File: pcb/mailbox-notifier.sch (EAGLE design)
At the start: 24 parts, among them Q1 AO3401, U1 MIC23155, U2 LTC2943-X, U3 FS312F-G, U4 FS8205, U5 MCP73832, U6 EFM32PG1B200_Q32, U7 RFM69HW

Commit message: PCB Work
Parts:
- removed U4: FS8205, Fortune:FS8205
- added C4: 100uF, Capacitor:CAPACITOR-1206
- added C49: 100nF, Capacitor:CAPACITOR-0603
- added CON1: 3P-SH-SIDE, JST:3P-SH-SIDE
- added D2: SMAJ5.0A, TVS:SMAJ5.0A
- added F1: 1A Hold, PTC Fuses:PTC1206
- added R1, R2: 5.1K Ohms, Resistor:RESISTOR-0603
- added R58: 1K Ohms, Resistor:RESISTOR-0603
- added R59: 100 Ohms, Resistor:RESISTOR-0603
- added R63: 10M Ohm, Resistor:RESISTOR-0603
- added U14: FS312F-G, Fortune:FS312F-G
- added U16: FS8205, Fortune:FS8205
- added U8: SI7021, Silicon Labs:SI7021
- U3: value FS312F-G -> 74LVC1G17; device Fortune:FS312F-G -> Logic:74LVC1G17
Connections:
- new net 5V0: C4.C1, D1.A, D2.C, F1.1, Q1.G
- new net EXT_TRIG: U3.1.Y
- new net GBAT: BAT1.-, C49.C2, R63.2, U14.GND, U16.S2
- new net N$2: BAT1.+, U2.VBAT/SENSE-
- new net N$3: R1.2, USB1.CC2
- new net N$4: F1.2, USB1.VBUS
- new net N$47: U14.OC, U16.G1
- new net N$48: U14.OD, U16.G2
- new net N$49: R59.1, U14.VCC
- new net N$5: R2.2, USB1.CC1
- new net N$50: R58.1, U14.CS
- new net N$6: CON1-2.S, U3.1.A
- new net VBAT: C49.C1, Q1.D, R59.2, U2.VDD/SENSE+
- new net VIN: D1.C, Q1.S
- net 2V8: now also CON1-1.S, U3.PWR.VCC
- net GND: now also C4.C2, CON1-3.S, D2.A, R1.1, R2.1, R58.2, R63.1, U16.S1, U3.PWR.GND, USB1.GND, USB1.SHIELD@0, USB1.SHIELD@1, USB1.SHIELD@2, USB1.SHIELD@3
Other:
- note added: "Decouple"

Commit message: PCB work
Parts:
- removed C49: 100nF, Capacitor:CAPACITOR-0603
- removed R58: 1K Ohms, Resistor:RESISTOR-0603
- removed R59: 100 Ohms, Resistor:RESISTOR-0603
- removed R63: 10M Ohm, Resistor:RESISTOR-0603
- removed U14: FS312F-G, Fortune:FS312F-G
- removed U16: FS8205, Fortune:FS8205
- removed U2: LTC2943-X, Analog Devices:LTC2943-X
- added C10: 2.2uF, Capacitor:CAPACITOR-0603
- added C11: 100uF, Capacitor:CAPACITOR-1206
- added C12, C14, C15, C20, C21, C23, C7: 100nF, Capacitor:CAPACITOR-0603
- added C17, C24: 1uF, Capacitor:CAPACITOR-0603
- added C22, C9: 470pF, Capacitor:CAPACITOR-0603
- added C5, C6: 10uF, Capacitor:CAPACITOR-0603
- added C8: 4.7uF, Capacitor:CAPACITOR-0603
- added D3: SK9822, LED:SK9822
- added L2: 4.7uH, Inductor:INDUCTOR-0603
- added R10: 324K Ohms, Resistor:RESISTOR-0603
- added R11: 91K Ohms, Resistor:RESISTOR-0603
- added R12: 10M Ohm, Resistor:RESISTOR-0603
- added R15: 10K Ohms, Resistor:RESISTOR-0603
- added R16, R17, R18, R19, R20, R9: 100K Ohms, Resistor:RESISTOR-0603
- added R21: 2K Ohms, Resistor:RESISTOR-0603
- added R3: 5.1K Ohms, Resistor:RESISTOR-0603
- added R7: 1K Ohms, Resistor:RESISTOR-0603
- added R8: 100 Ohms, Resistor:RESISTOR-0603
- added U10: SI7021, Silicon Labs:SI7021
- added U12: MIC2019, Microchip:MIC2019
- added U4: MIC23155, Microchip:MIC23155
- added U9: RFM69HW, HopeRF:RFM69HW
- added X1: 40MHz, Crystal:CRYSTAL_4P
- C16: value 100nF -> 4.7uF
- C18: value 1uF -> 100nF
- C19: value 4.7uF -> 100nF
- C2: value 100nF -> 100uF; device Capacitor:CAPACITOR-0603 -> Capacitor:CAPACITOR-1206
- D1: value B0530W -> SMAJ5.0A; device Generic Diode:B0530W -> TVS:SMAJ5.0A
- D2: value SMAJ5.0A -> B0530W; device TVS:SMAJ5.0A -> Generic Diode:B0530W
- L1: value 4.7uH -> 2.2uH; device Inductor:INDUCTOR-0603 -> Inductor:INDUCTOR-0805; OCLCSC C281111 -> C139241
- R13, R4: value 10K Ohms -> 100K Ohms
- R2: value 5.1K Ohms -> 2.2K Ohms
- U1: value MIC23155 -> MCP73832; device Microchip:MIC23155 -> Microchip:MCP73832
- U5: value MCP73832 -> FS312F-G; device Microchip:MCP73832 -> Fortune:FS312F-G
- U6: value EFM32PG1B200_Q32 -> FS8205; device EFM32:EFM32PG1B200_Q32 -> Fortune:FS8205
- U7: value RFM69HW -> EFM32PG1B200_Q32; device HopeRF:RFM69HW -> EFM32:EFM32PG1B200_Q32
- U8: value SI7021 -> SST26VF016B; device Silicon Labs:SI7021 -> Microchip:SST26VF016B
- renumbered C1 to C13, U3 to U11
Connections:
- removed net N$2: BAT1.+, U2.VBAT/SENSE-
- new net !FLASH_CS: R16.1, U8.!CS!
- new net 2V8_PGOOD: R9.1, U4.PG
- new net BAT_STAT: R4.1, U1.STAT
- new net I2C0_SCL: R15.1, U10.SCL
- new net I2C0_SDA: R14.1, U10.SDA
- new net LED_EN: U12.EN
- new net N$10: R2.2, U1.PROG
- new net N$11: R21.2, U12.ILIMIT
- new net N$12: L1.1, U4.SW
- new net N$13: R10.1, R11.2, U4.FB
- new net N$14: C9.C1, U4.SS
- new net N$15: C24.C1, D3.VDD@5, U12.VOUT
- new net N$16: U7.HFXTAL_N, X1.1
- new net N$17: U7.HFXTAL_P, X1.2
- new net US1_CLK: D3.CLKI@4
- new net US1_MOSI: D3.SDI@3
- new net VBAT_SENSE: C22.C1, R19.1, R20.2
- new net VIN1: C3.C1
- net !RFM_CS: now also R18.1, U7.PD12, U9.!CS; no longer R14.1, U6.PD12, U7.!CS
- net !RST: now also R13.1, U7.!RESET; no longer R4.1, U6.!RESET
- net 1V8: now also C16.C1, L2.1, U7.DVDD; no longer C19.C1, L1.1, U6.DVDD
- net 2V8: now also C10.C1, C11.C1, C14.C1, C15.C1, C18.C1, C19.C2, C20.C1, C21.C1, C23.C1, L1.2, R10.2, R13.2, R15.2, R16.2, R18.2, R9.2, U10.VDD, U12.VIN, U4.SNS, U7.AVDD@0, U7.AVDD@1, U7.IOVDD0@0, U7.VREGVDD, U8.!HOLD!/IO3, U8.!WP!/IO2, U8.VCC, U9.VCC; no longer C16.C2, C2.C1, C3.C1, U6.AVDD@0, U6.AVDD@1, U6.IOVDD0@0, U6.VREGVDD, U7.VCC
- net 5V0: now also C2.C1, D1.C, D2.A, U1.VDD; no longer C4.C1, D1.A, D2.C
- net GBAT: now also C12.C2, R12.2, U5.GND, U6.S2; no longer C49.C2, R63.2, U14.GND, U16.S2
- net GND: now also C10.C2, C11.C2, C14.C2, C15.C2, C16.C2, C17.C1, C18.C2, C19.C1, C20.C2, C21.C2, C22.C2, C23.C2, C24.C2, C5.C2, C6.C2, C7.C2, C8.C2, C9.C2, D1.A, D3.GND@2, R11.1, R12.1, R17.1, R20.1, R21.1, R3.1, R7.1, U1.VSS, U10.GND, U12.GND, U4.AGND, U4.PGND@0, U4.PGND@1, U6.S1, U7.VREGVSS, U7.VSS@0, U8.GND, U9.GND, X1.GND@0, X1.GND@1; no longer C16.C1, C18.C1, C19.C2, D2.A, R13.1, R58.2, R63.1, U16.S1, U6.VREGVSS, U6.VSS@0, U7.GND
- net N$1: now also U9.ANT; no longer U7.ANT
- net N$19: now also L2.2, U7.VREGSW; no longer L1.2, U6.VREGSW
- net N$20: now also C17.C2, U7.DECOUPLE; no longer C18.C2, U6.DECOUPLE
- net N$47: now also U5.OC, U6.G1; no longer U14.OC, U16.G1
- net N$48: now also U5.OD, U6.G2; no longer U14.OD, U16.G2
- net N$49: now also R8.1, U5.VCC; no longer R59.1, U14.VCC
- net N$5: now also R3.2; no longer R2.2
- net N$50: now also R7.2, U5.CS; no longer R58.1, U14.CS
- net RFM_IRQ: now also U7.PC10, U9.IO0; no longer U6.PC10, U7.IO0
- net RFM_RST: now also R17.2, U7.PD11, U9.RST; no longer R13.2, U6.PD11, U7.RST
- net SWCLK: now also U7.PF0; no longer U6.PF0
- net SWDIO: now also U7.PF1; no longer U6.PF1
- net SWO: now also U7.PF2; no longer U6.PF2
- net US0_CLK: now also U7.PD13, U8.SCK, U9.SCK; no longer U6.PD13, U7.SCK
- net US0_MISO: now also U7.PD15, U8.MISO/IO1, U9.MISO; no longer U6.PD15, U7.MISO
- net US0_MOSI: now also U7.PD14, U8.MOSI/IO0, U9.MOSI; no longer U6.PD14, U7.MOSI
- net VBAT: now also BAT1.+, C12.C1, C4.C1, R19.2, R8.2, U1.VBAT; no longer C49.C1, R59.2, U2.VDD/SENSE+
- net VIN: now also C5.C1, C6.C1, C7.C1, C8.C1, D2.C, U4.EN, U4.VIN@0, U4.VIN@1; no longer D1.C

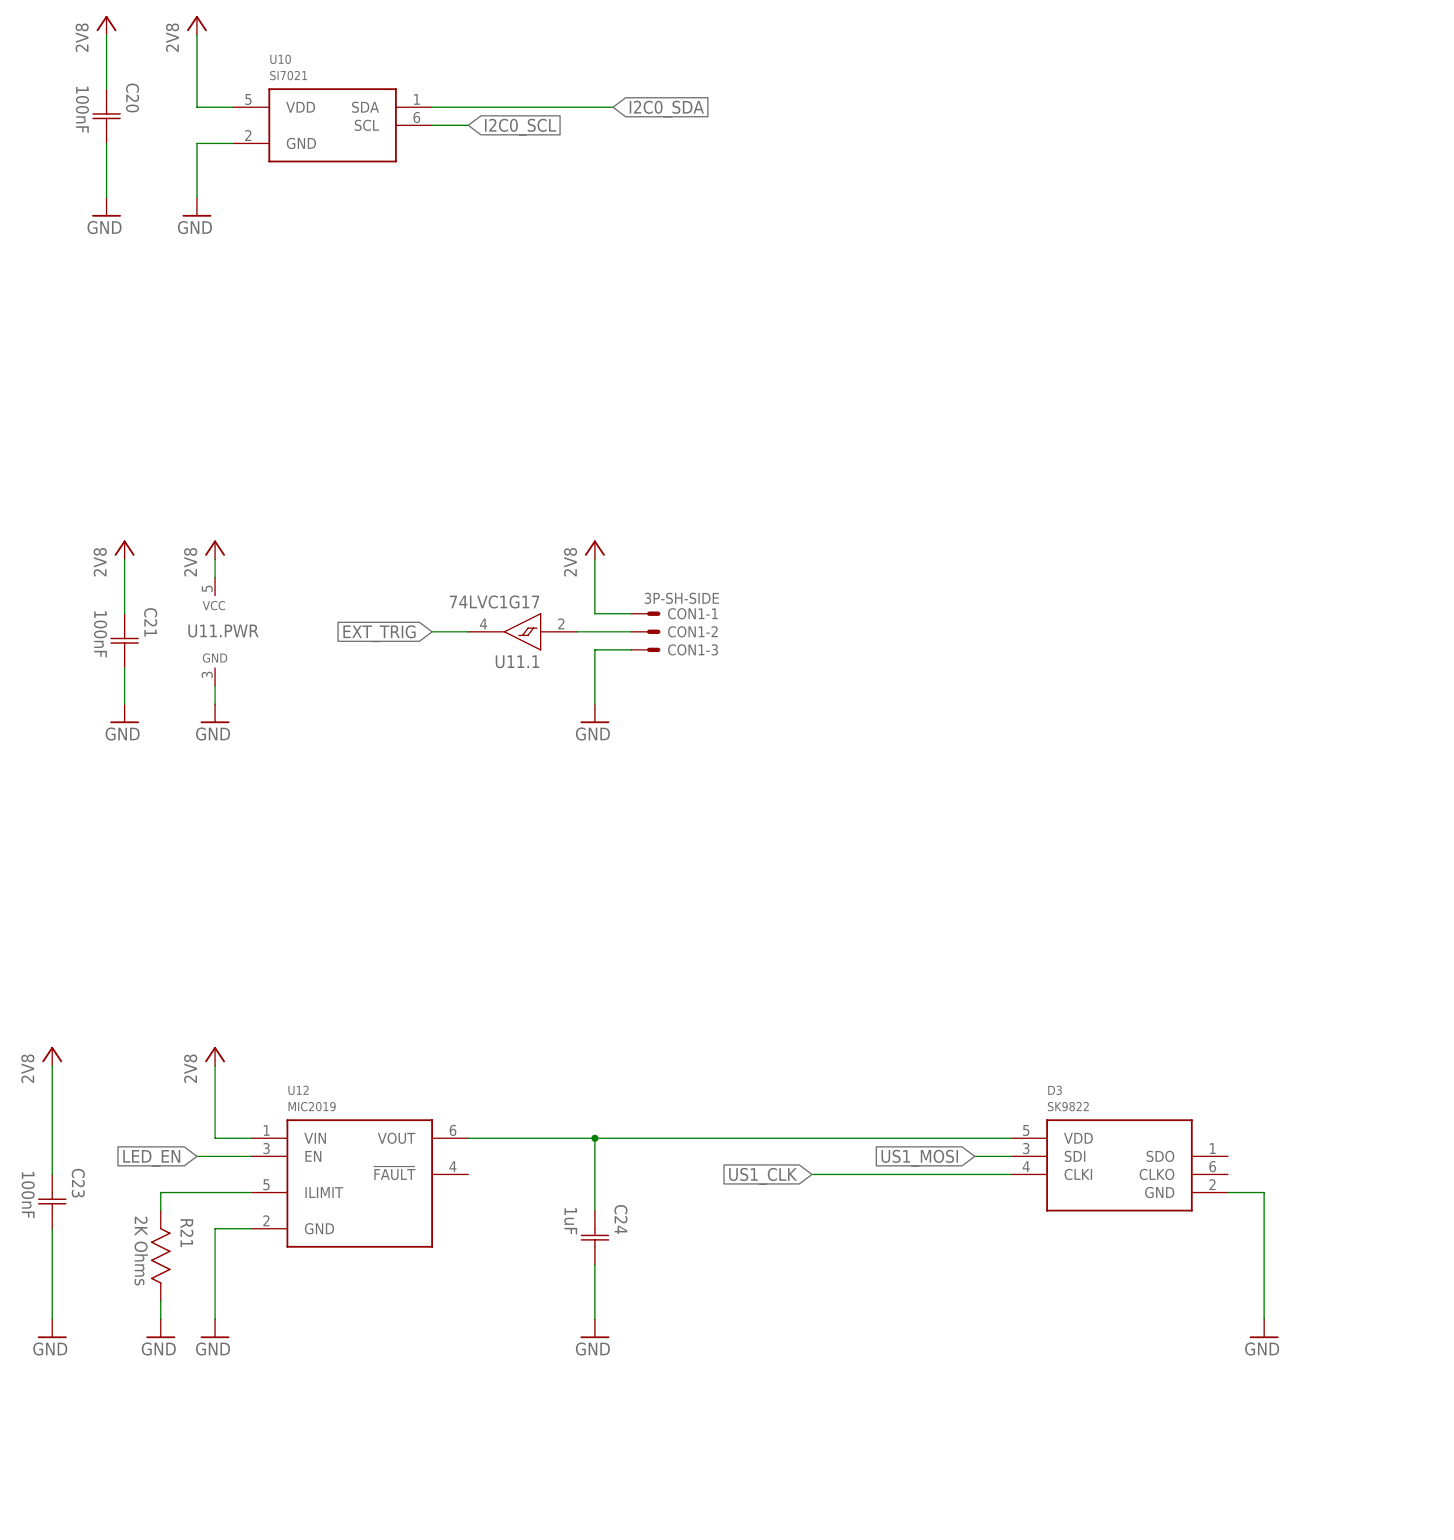
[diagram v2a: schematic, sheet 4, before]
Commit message: Add power switch to external trigger
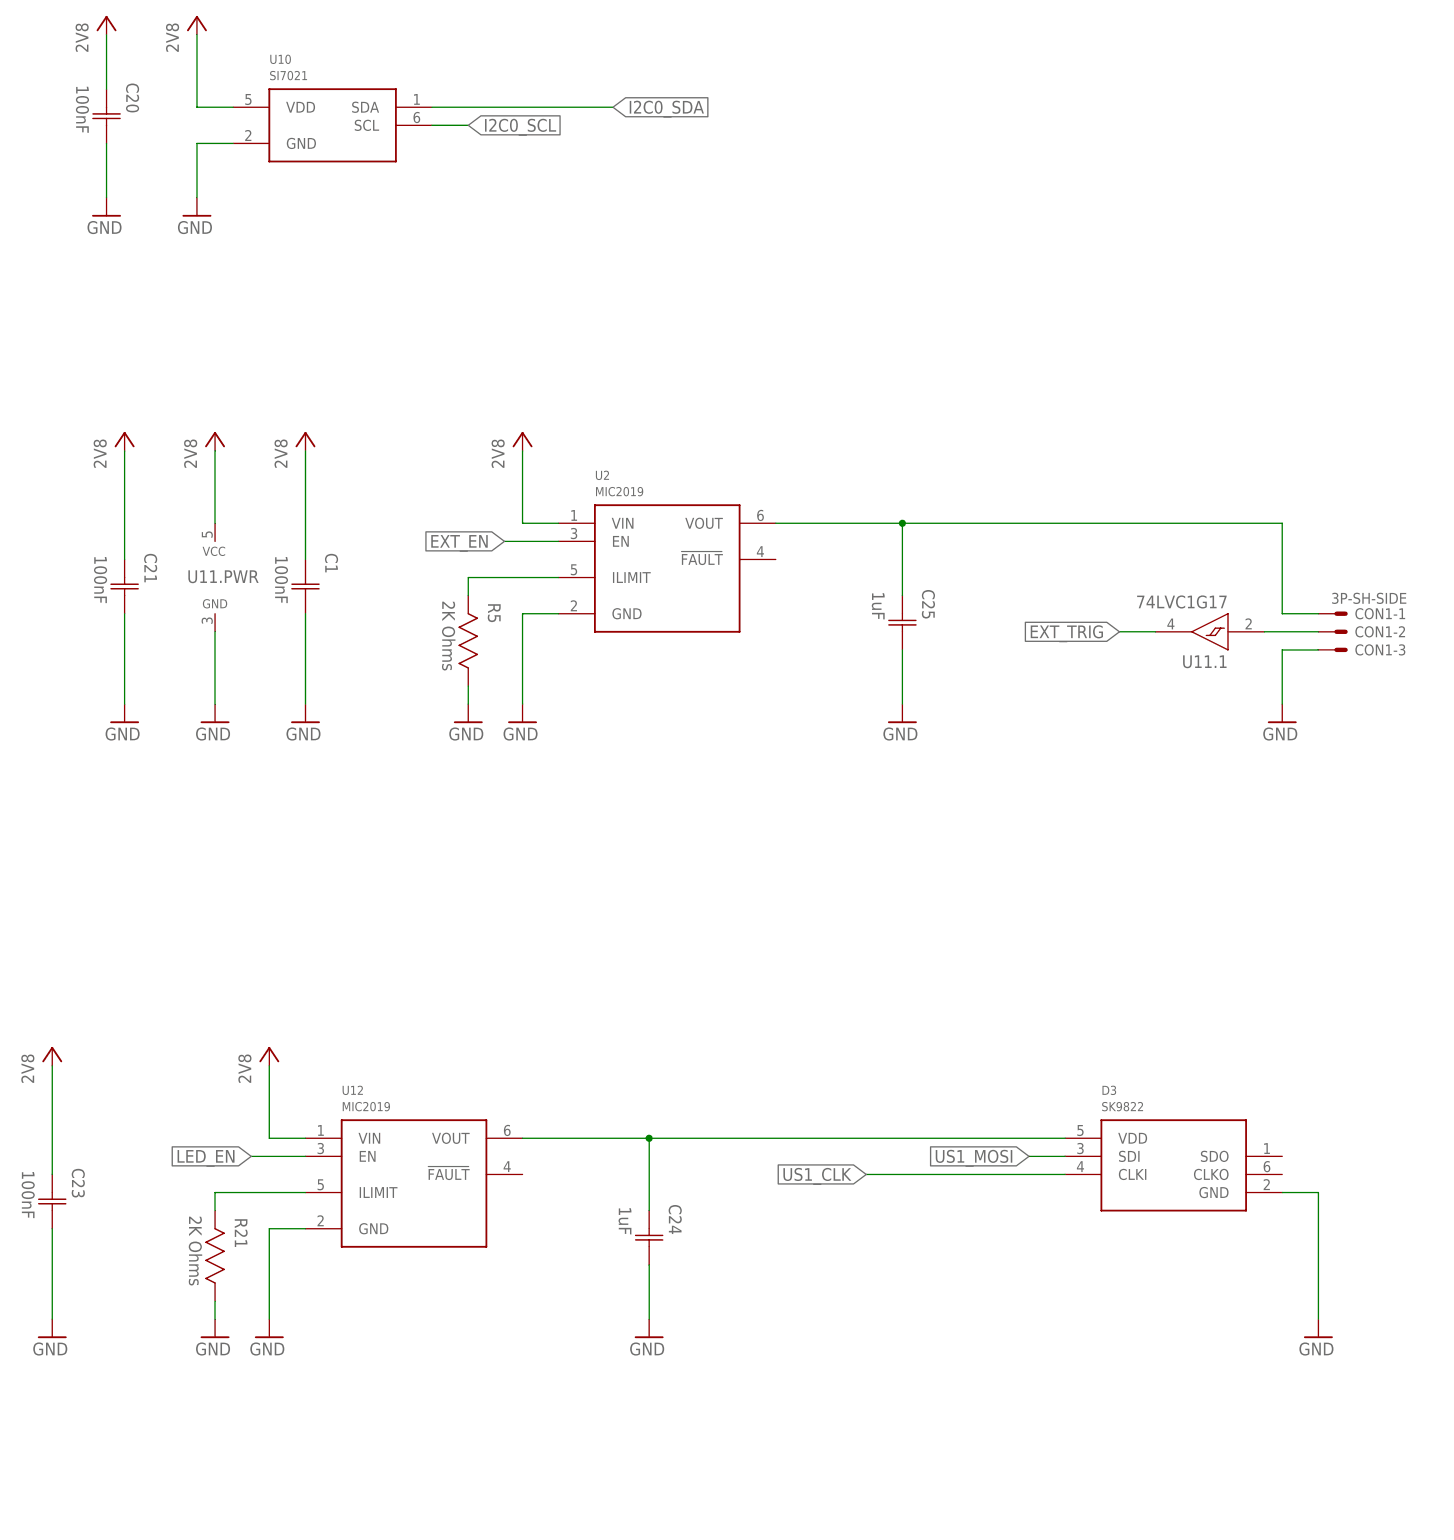
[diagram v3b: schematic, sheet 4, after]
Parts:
- added C1: 100nF, Capacitor:CAPACITOR-0603
- added C25: 1uF, Capacitor:CAPACITOR-0603
- added R5: 2K Ohms, Resistor:RESISTOR-0603
- added U2: MIC2019, Microchip:MIC2019
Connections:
- new net EXT_EN: U2.EN
- new net N$2: R5.2, U2.ILIMIT
- new net N$7: C25.C1, CON1-1.S, U2.VOUT
- net 2V8: now also C1.C1, U2.VIN; no longer CON1-1.S
- net GND: now also C1.C2, C25.C2, R5.1, U2.GND
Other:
- moved on the sheet: C21, C24, CON1-1, CON1-2, CON1-3, D3, R21, U11.1, U11.PWR, U12

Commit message: PCB work
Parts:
- removed C24, C25: 1uF, Capacitor:CAPACITOR-0603
- removed R21: 2K Ohms, Resistor:RESISTOR-0603
- removed U12: MIC2019, Microchip:MIC2019
- added R6: 100K Ohms, Resistor:RESISTOR-0603
- added U3: FS312F-G, Fortune:FS312F-G
- C10: value 2.2uF -> 100uF; device Capacitor:CAPACITOR-0603 -> Capacitor:CAPACITOR-1206
- C11: value 100uF -> 100nF; device Capacitor:CAPACITOR-1206 -> Capacitor:CAPACITOR-0603
- C15: value 100nF -> 4.7uF
- C16: value 4.7uF -> 1uF
- C17: value 1uF -> 100nF
- C22: value 470pF -> 1uF
- C23: value 100nF -> 1uF
- C3: value 100nF -> 100uF; device Capacitor:CAPACITOR-0603 -> Capacitor:CAPACITOR-1206
- C4: value 100uF -> 10uF; device Capacitor:CAPACITOR-1206 -> Capacitor:CAPACITOR-0603
- C6: value 10uF -> 470pF
- C8: value 4.7uF -> 470pF
- C9: value 470pF -> 2.2uF
- R19, R20: value 100K Ohms -> 2K Ohms
- R5: value 2K Ohms -> 100K Ohms
- U10: value SI7021 -> MIC2019; device Silicon Labs:SI7021 -> Microchip:MIC2019
- U2: value MIC2019 -> MIC23155; device Microchip:MIC2019 -> Microchip:MIC23155
- U4: value MIC23155 -> FS8205; device Microchip:MIC23155 -> Fortune:FS8205
- U5: value FS312F-G -> EFM32PG1B200F256GM32; device Fortune:FS312F-G -> EFM32:EFM32PG1B200F256GM32
- U6: value FS8205 -> SST26VF016B; device Fortune:FS8205 -> Microchip:SST26VF016B
- U7: value EFM32PG1B200_Q32 -> RFM69HW; device EFM32:EFM32PG1B200_Q32 -> HopeRF:RFM69HW
- U8: value SST26VF016B -> SI7021; device Microchip:SST26VF016B -> Silicon Labs:SI7021
- U9: value RFM69HW -> MIC2019; device HopeRF:RFM69HW -> Microchip:MIC2019
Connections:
- removed net VIN1: C3.C1
- net !FLASH_CS: now also U5.PD15, U6.!CS!; no longer U8.!CS!
- net !RFM_CS: now also U5.PD13, U7.!CS; no longer U7.PD12, U9.!CS
- net !RST: now also U5.!RESET; no longer U7.!RESET
- net 1V8: now also C15.C1, U5.DVDD; no longer C16.C1, U7.DVDD
- net 2V8: now also C12.C1, C17.C1, C18.C2, C19.C1, C9.C1, U10.VIN, U2.SNS, U5.AVDD@0, U5.AVDD@1, U5.IOVDD0@0, U5.VREGVDD, U6.!HOLD!/IO3, U6.!WP!/IO2, U6.VCC, U7.VCC, U8.VDD, U9.VIN; no longer C1.C1, C11.C1, C15.C1, C18.C1, C19.C2, C23.C1, U10.VDD, U12.VIN, U2.VIN, U4.SNS, U7.AVDD@0, U7.AVDD@1, U7.IOVDD0@0, U7.VREGVDD, U8.!HOLD!/IO3, U8.!WP!/IO2, U8.VCC, U9.VCC
- net 2V8_PGOOD: now also U2.PG, U5.PF3; no longer U4.PG
- net BAT_STAT: now also U5.PC10
- net EXT_EN: now also U10.EN, U5.PB14; no longer U2.EN
- net EXT_TRIG: now also U5.PB15
- net GBAT: now also C11.C2, U3.GND, U4.S2; no longer C12.C2, U5.GND, U6.S2
- net GND: now also C12.C2, C16.C1, C17.C2, C18.C1, C19.C2, R19.1, R6.1, U2.AGND, U2.PGND@0, U2.PGND@1, U4.S1, U5.VREGVSS, U5.VSS@0, U6.GND, U7.GND; no longer C11.C2, C16.C2, C17.C1, C18.C2, C19.C1, C24.C2, C25.C2, R21.1, R5.1, U12.GND, U2.GND, U4.AGND, U4.PGND@0, U4.PGND@1, U6.S1, U7.VREGVSS, U7.VSS@0
- net I2C0_SCL: now also U5.PB13, U8.SCL; no longer U10.SCL
- net I2C0_SDA: now also U5.PB12, U8.SDA; no longer U10.SDA
- net LED_EN: now also U5.PB11, U9.EN; no longer U12.EN
- net N$1: now also U7.ANT; no longer U9.ANT
- net N$11: now also R19.2, U9.ILIMIT; no longer R21.2, U12.ILIMIT
- net N$12: now also U2.SW; no longer U4.SW
- net N$13: now also U2.FB; no longer U4.FB
- net N$14: now also C8.C1, U2.SS; no longer C9.C1, U4.SS
- net N$15: now also C22.C1, U9.VOUT; no longer C24.C1, U12.VOUT
- net N$16: now also U5.HFXTAL_N; no longer U7.HFXTAL_N
- net N$17: now also U5.HFXTAL_P; no longer U7.HFXTAL_P
- net N$19: now also U5.VREGSW; no longer U7.VREGSW
- net N$2: now also R20.2, U10.ILIMIT; no longer R5.2, U2.ILIMIT
- net N$20: now also C16.C2, U5.DECOUPLE; no longer C17.C2, U7.DECOUPLE
- net N$47: now also U3.OC, U4.G1; no longer U5.OC, U6.G1
- net N$48: now also U3.OD, U4.G2; no longer U5.OD, U6.G2
- net N$49: now also U3.VCC; no longer U5.VCC
- net N$50: now also U3.CS; no longer U5.CS
- net N$7: now also C23.C1, U10.VOUT; no longer C25.C1, U2.VOUT
- net RFM_IRQ: now also U5.PD14, U7.IO0; no longer U7.PC10, U9.IO0
- net RFM_RST: now also U5.PD12, U7.RST; no longer U7.PD11, U9.RST
- net SWCLK: now also U5.PF0; no longer U7.PF0
- net SWDIO: now also U5.PF1; no longer U7.PF1
- net SWO: now also U5.PF2; no longer U7.PF2
- net US0_CLK: now also U5.PD9, U6.SCK, U7.SCK; no longer U7.PD13, U8.SCK, U9.SCK
- net US0_MISO: now also U5.PD11, U6.MISO/IO1, U7.MISO; no longer U7.PD15, U8.MISO/IO1, U9.MISO
- net US0_MOSI: now also U5.PD10, U6.MOSI/IO0, U7.MOSI; no longer U7.PD14, U8.MOSI/IO0, U9.MOSI
- net US1_CLK: now also U5.PA1
- net US1_MOSI: now also U5.PA0
- net VBAT: now also C1.C1, C11.C1, C3.C1, R5.2; no longer C12.C1, C4.C1, R19.2
- net VBAT_SENSE: now also C6.C1, R5.1, R6.2, U5.PC11; no longer C22.C1, R19.1, R20.2
- net VIN: now also C4.C1, U2.EN, U2.VIN@0, U2.VIN@1; no longer C6.C1, C8.C1, U4.EN, U4.VIN@0, U4.VIN@1
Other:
- moved on the sheet: C10, C11, C13, C14, C15, C16, C17, C21, C23, C3, C4, C5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
